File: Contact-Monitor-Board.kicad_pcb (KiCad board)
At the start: 2 copper layers, 100 x 100 mm, 83 parts, among them J1 JST VH 02, J10 JST VH 02, J11 JST VH 02, J12 JST VH 02, J13 JST VH 02, J14 JST VH 02, J15 JST VH 02, J16 JST VH 02, J17 header 4, J2 JST VH 02, J3 JST VH 02, J4 JST VH 02, J5 JST VH 02, J6 JST VH 02, J7 JST VH 02, J8 JST VH 02, J9 JST VH 02, Q1 2N7002, Q10 2N7002, Q11 2N7002, Q12 2N7002, Q13 2N7002, Q14 2N7002, Q15 2N7002, Q16 2N7002, Q2 2N7002, Q3 2N7002, Q4 2N7002, Q5 2N7002, Q6 2N7002, Q7 2N7002, Q8 2N7002, Q9 2N7002, SW1 KH-SS12D01-G3-5.0, U1 74HC4017D, U2 TLC555CD, U3 TPS61222DCK

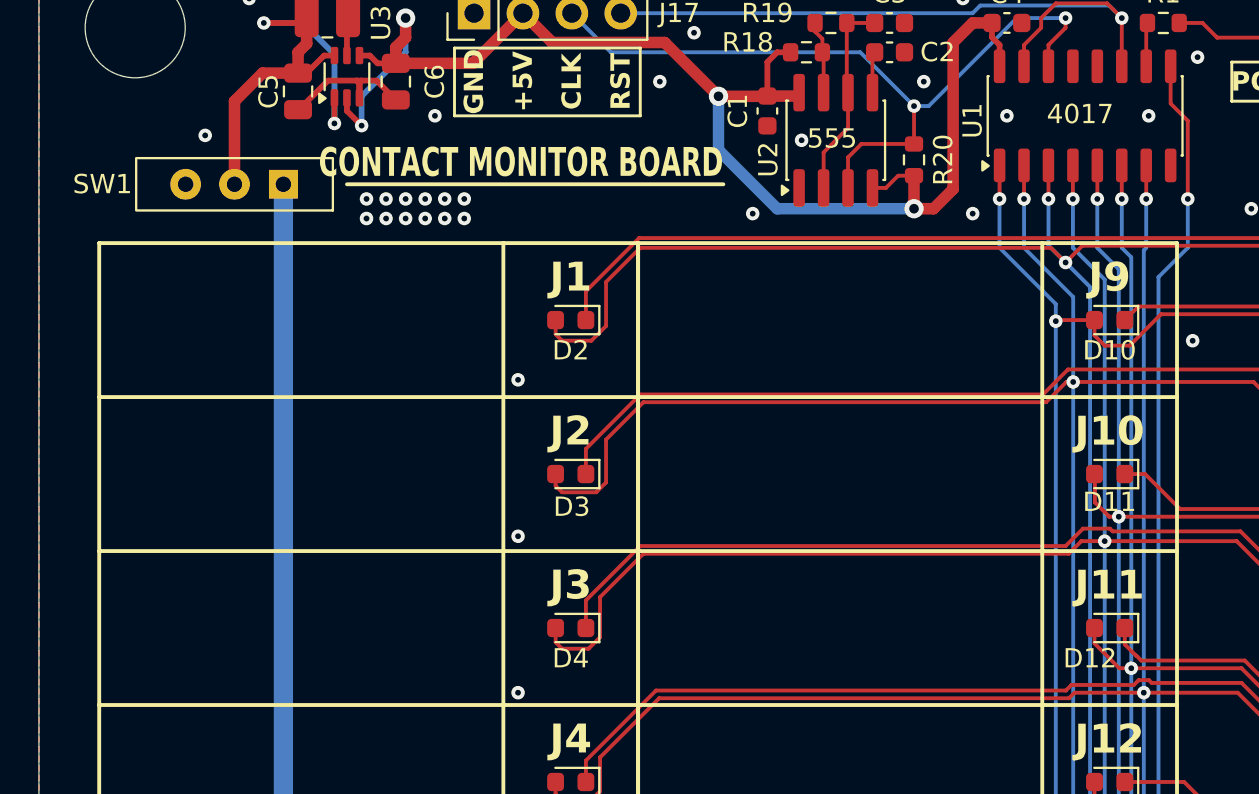
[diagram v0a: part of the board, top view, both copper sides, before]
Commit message: V1.3.1 電池ケース裏面のランド追加とシルク・寸法注記の整備
- BT1 のスルーホールパッドを "*.Cu" "*.Mask" に変更し、裏面にランドと
  マスク開口を追加（従来は F.Mask のみで裏面が露出していなかった）。
  THT なので F.Paste は削除。ライブラリと基板の双方を更新
- 運転 LED の輝度を再調整し R1 を 470 に戻す。README の
  「抵抗は 470 Ω と 4.7 kΩ の 2 種類」の構成と整合させる
- タイトルシルクを knockout 化し、下線をドットに変更
- 取付穴 4-φ5.2 と外形寸法の注記を Cmts.User に追加
- rev を 1.3.1 に更新し、ガーバー / BOM / CPL / PDF を再生成
- 基板レンダリング画像（表・裏）を追加

DRC: 違反 0 / 未配線 0 / 回路図パリティ 0

Co-Authored-By: Claude Opus 5 <noreply@anthropic.com>
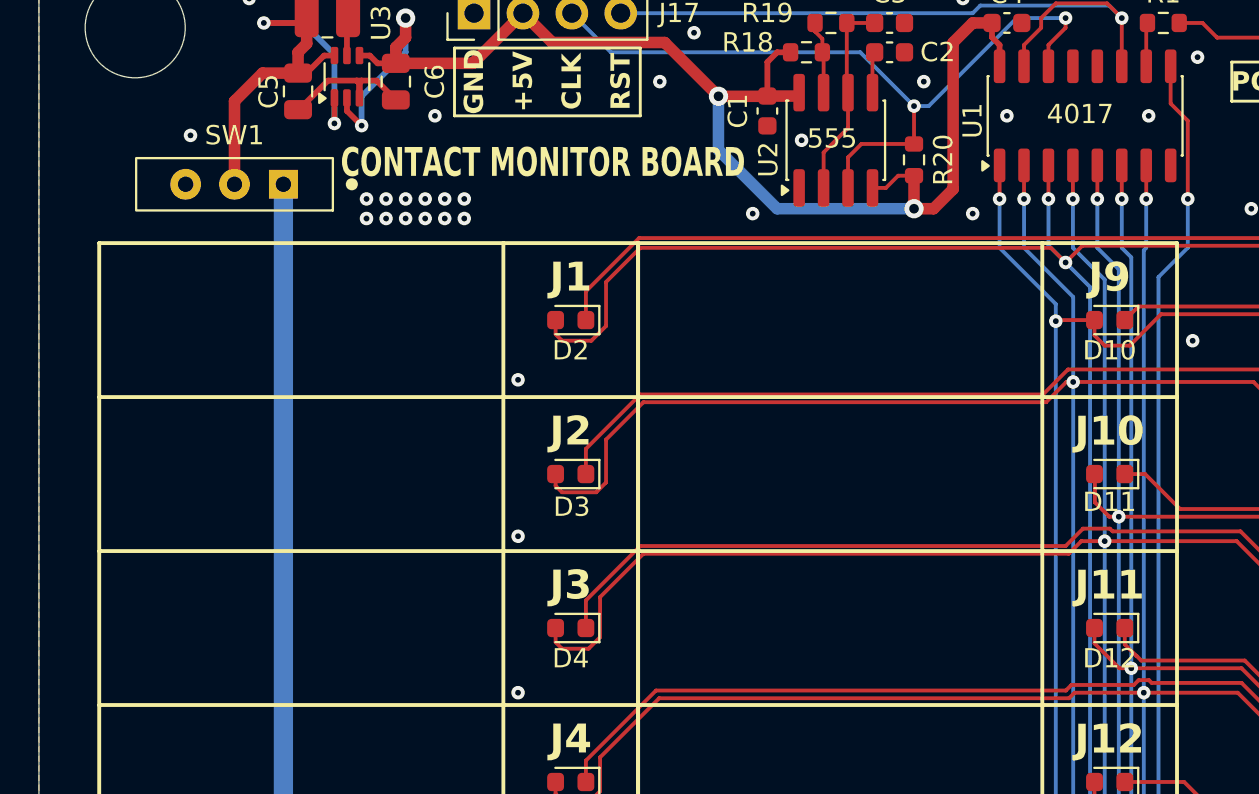
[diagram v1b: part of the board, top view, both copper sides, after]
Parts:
- R1: value 1.0k -> 470
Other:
- board text added: "4-φ5.2"
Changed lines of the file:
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@@
 	(title_block
 		(title "Contact Monitor Board")
-		(date "2026-08-13")
-		(rev "1.3")
+		(date "2026-08-19")
+		(rev "1.3.1")
 		(company "Satoru Yamaguchi")
 		(comment 1 "Copyright (c) 2026 Satoru Yamaguchi")
@@
 		(tags "switch single-pole opposite-side-connection double-throw SPDT würth wurth")
 		(property "Reference" "SW1"
-			(at 6.858 0 180)
+			(at 0 2.54 180)
 			(layer "F.SilkS")
 			(effects
@@
 		(tags "LED")
 		(property "Reference" "D12"
-			(at 1.02 -1.582 0)
+			(at 0.004 -1.582 0)
 			(layer "F.SilkS")
 			(effects
@@
 			)
 		)
-		(property "Value" "1.0k"
+		(property "Value" "470"
 			(at 0 1.43 0)
 			(layer "F.Fab")
@@
 			)
 		)
-		(property "LCSC" "C21190"
+		(property "LCSC" "C23179"
 			(at 0 0 0)
 			(layer "F.SilkS")
@@
 			(size 1.8 1.8)
 			(drill 1.2)
-			(layers "*.Cu" "F.Mask" "F.Paste")
+			(layers "*.Cu" "*.Mask")
 			(remove_unused_layers no)
 			(net 69 "Net-(BT1-PLUS)")
@@
 			(size 1.8 1.8)
 			(drill 1.2)
-			(layers "*.Cu" "F.Mask" "F.Paste")
+			(layers "*.Cu" "*.Mask")
 			(remove_unused_layers no)
 			(net 19 "GND")
@@
 		(layer "F.SilkS")
 	)
-	(gr_line
-		(start 86.002 46.132)
-		(end 105.56 46.132)
+	(gr_circle
+		(center 86.256 46.132)
+		(end 86.51 46.132)
 		(stroke
-			(width 0.2)
+			(width 0.12)
 			(type default)
 		)
+		(fill yes)
 		(layer "F.SilkS")
 	)
@@
 	)
 	(gr_line
+		(start 65.936 137.826)
+		(end 72.54 130.46)
+		(stroke
+			(width 0.1)
+			(type default)
+		)
+		(layer "Cmts.User")
+	)
+	(gr_line
+		(start 72.54 130.46)
+		(end 71.27 130.46)
+		(stroke
+			(width 0.1)
+			(type default)
+		)
+		(layer "Cmts.User")
+	)
+	(gr_line
+		(start 72.54 130.46)
+		(end 72.54 131.73)
+		(stroke
+			(width 0.1)
+			(type default)
+		)
+		(layer "Cmts.User")
+	)
+	(gr_line
 		(start 70 35.999999)
 		(end 69.999999 130)
@@
 	)
 	(gr_text "CONTACT MONITOR BOARD"
-		(at 105.56 45.878 0)
-		(layer "F.SilkS")
+		(at 106.703 45.878 0)
+		(layer "F.SilkS" knockout)
 		(effects
 			(font
@@
 		)
 	)
+	(gr_text "4-φ5.2"
+		(at 47.902 142.652 0)
+		(layer "Cmts.User")
+		(effects
+			(font
+				(size 3 3)
+				(thickness 0.15)
+			)
+			(justify left bottom)
+		)
+	)
+	(dimension
+		(type orthogonal)
+		(layer "Cmts.User")
+		(pts
+			(xy 70 133) (xy 165 128)
+		)
+		(height -4.826)
+		(orientation 1)
+		(format
+			(prefix "")
+			(suffix "")
+			(units 3)
+			(units_format 0)
+			(precision 4)
+			(suppress_zeroes yes)
+		)
+		(style
+			(thickness 0.1)
+			(arrow_length 1.27)
+			(text_position_mode 0)
+			(arrow_direction outward)
+			(extension_height 0.58642)
+			(extension_offset 0.5)
+			(keep_text_aligned yes)
+		)
+		(gr_text "5"
+			(at 64.024 130.5 90)
+			(layer "Cmts.User")
+			(effects
+				(font
+					(size 1 1)
+					(thickness 0.15)
+				)
+			)
+		)
+	)
+	(dimension
+		(type orthogonal)
+		(layer "Cmts.User")
+		(pts
+			(xy 165 38) (xy 165 128)
+		)
+		(height -99.826)
+		(orientation 1)
+		(format
+			(prefix "")
+			(suffix "")
+			(units 3)
+			(units_format 0)
+			(precision 4)
+			(suppress_zeroes yes)
+		)
+		(style
+			(thickness 0.1)
+			(arrow_length 1.27)
+			(text_position_mode 0)
+			(arrow_direction outward)
+			(extension_height 0.58642)
+			(extension_offset 0.5)
+			(keep_text_aligned yes)
+		)
+		(gr_text "90"
+			(at 64.024 83 90)
+			(layer "Cmts.User")
+			(effects
+				(font
+					(size 1 1)
+					(thickness 0.15)
+				)
+			)
+		)
+	)
 	(dimension
 		(type orthogonal)
@@
 		(layer "Cmts.User")
 		(pts
-			(xy 71 133) (xy 71 33)
+			(xy 70 133) (xy 70 33)
 		)
 		(height -9.5)
@@
 		)
 		(gr_text "100"
-			(at 60.35 83 90)
+			(at 59.35 83 90)
 			(layer "Cmts.User")
 			(effects
@@
 	)
 	(via
-		(at 157.63 77.882)
+		(at 89.05 46.894)
 		(size 0.7)
 		(drill 0.3)
@@
 	)
 	(via
-		(at 166.012 103.028)
+		(at 157.63 77.882)
 		(size 0.7)
 		(drill 0.3)
@@
 	)
 	(via
-		(at 94.892 96.17)
+		(at 166.012 103.028)
 		(size 0.7)
 		(drill 0.3)
@@
 	)
 	(via
-		(at 90.066 47.91)
+		(at 94.892 96.17)
 		(size 0.7)
 		(drill 0.3)
@@
 	)
 	(via
-		(at 134.77 70.262)
+		(at 90.066 47.91)
 		(size 0.7)
 		(drill 0.3)
@@
 	)
 	(via
-		(at 88.034 47.91)
+		(at 134.77 70.262)
 		(size 0.7)
 		(drill 0.3)
@@
 	)
 	(via
-		(at 87.018 46.894)
+		(at 88.034 47.91)
 		(size 0.7)
 		(drill 0.3)
@@
 	)
 	(via
-		(at 159.662 42.068)
+		(at 90.066 46.894)
 		(size 0.7)
 		(drill 0.3)
@@
 	)
 	(via
-		(at 91.082 46.894)
+		(at 159.662 42.068)
 		(size 0.7)
 		(drill 0.3)
@@
 	)
 	(via
+		(at 92.098 46.894)
+		(size 0.7)
+		(drill 0.3)
+		(layers "F.Cu" "B.Cu")
+		(free yes)
+		(net 19)
+	)
+	(via
 		(at 89.05 47.91)
 		(size 0.7)
@@
 	)
 	(via
-		(at 88.034 46.894)
-		(size 0.7)
-		(drill 0.3)
-		(layers "F.Cu" "B.Cu")
-		(free yes)
-		(net 19)
-	)
-	(via
 		(at 87.018 47.91)
 		(size 0.7)
@@
 	)
 	(via
+		(at 91.082 46.894)
+		(size 0.7)
+		(drill 0.3)
+		(layers "F.Cu" "B.Cu")
+		(free yes)
+		(net 19)
+	)
+	(via
+		(at 87.018 46.894)
+		(size 0.7)
+		(drill 0.3)
+		(layers "F.Cu" "B.Cu")
+		(free yes)
+		(net 19)
+	)
+	(via
 		(at 107.084 47.656)
 		(size 0.7)
@@
 	)
 	(via
+		(at 88.034 46.894)
+		(size 0.7)
+		(drill 0.3)
+		(layers "F.Cu" "B.Cu")
+		(free yes)
+		(net 19)
+	)
+	(via
 		(at 136.04 47.91)
 		(size 0.7)
@@
 	)
 	(via
-		(at 78.636 43.592)
+		(at 77.874 43.592)
 		(size 0.7)
 		(drill 0.3)
@@
 	)
 	(via
-		(at 90.066 46.894)
-		(size 0.7)
-		(drill 0.3)
-		(layers "F.Cu" "B.Cu")
-		(free yes)
-		(net 19)
-	)
-	(via
 		(at 166.012 62.896)
 		(size 0.7)
@@
 	)
 	(via
-		(at 92.098 46.894)
-		(size 0.7)
-		(drill 0.3)
-		(layers "F.Cu" "B.Cu")
-		(free yes)
-		(net 19)
-	)
-	(via
 		(at 104.544 114.966)
 		(size 0.7)
@@
 		(size 0.7)
 		(drill 0.3)
-		(layers "F.Cu" "B.Cu")
-		(free yes)
-		(net 19)
-	)
-	(via
-		(at 89.05 46.894)
-		(size 0.7)
-		(drill 0.3)
